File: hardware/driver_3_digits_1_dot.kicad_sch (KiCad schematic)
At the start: 11 parts, among them U4 HV5622PG

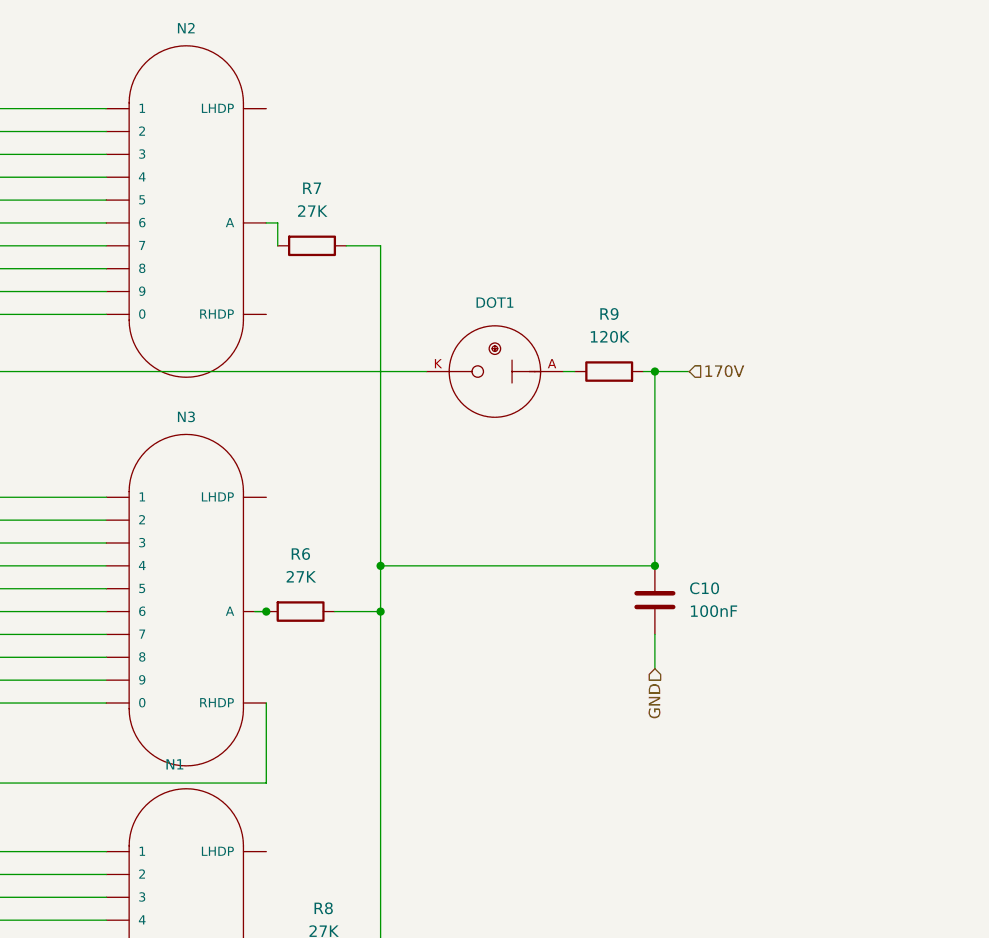
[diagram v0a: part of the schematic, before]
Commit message: Add HT psu.
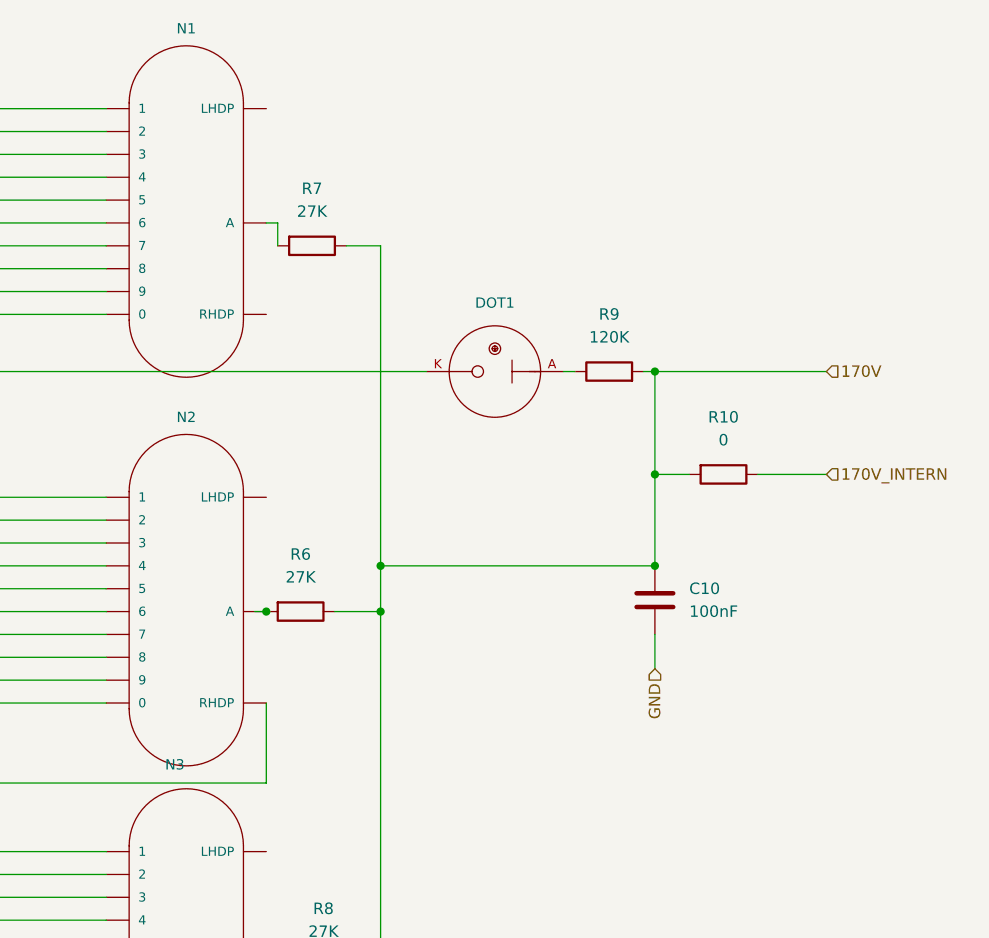
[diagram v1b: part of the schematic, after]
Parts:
- added R10: 0, Resistor_SMD:R_1206_3216Metric, symbol Device:R
- renumbered N2 to N1, N3 to N2, N1 to N3
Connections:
- net 170V: now also R10.2
- new net 170V_INTERN: R10.1
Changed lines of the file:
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@@
+	)
+	(junction
+		(at 182.88 72.39)
+		(diameter 0)
+		(color 0 0 0 0)
+	)
+	(junction
+		(at 152.4 82.55)
+		(diameter 0)
+		(color 0 0 0 0)
 	)
 	(junction
@@
 	)
 	(junction
-		(at 152.4 82.55)
-		(diameter 0)
-		(color 0 0 0 0)
-	)
-	(junction
 		(at 152.4 87.63)
 		(diameter 0)
@@
 	(wire
 		(pts
-			(xy 182.88 60.96) (xy 186.69 60.96)
-		)
-		(stroke
-			(width 0)
-			(type default)
-		)
-	)
-	(wire
-		(pts
 			(xy 148.59 46.99) (xy 152.4 46.99)
 		)
@@
 	(wire
 		(pts
-			(xy 182.88 60.96) (xy 182.88 82.55)
-		)
-		(stroke
-			(width 0)
-			(type default)
-		)
-	)
-	(wire
-		(pts
 			(xy 87.63 85.09) (xy 121.92 85.09)
 		)
@@
 	(wire
 		(pts
+			(xy 182.88 60.96) (xy 182.88 72.39)
+		)
+		(stroke
+			(width 0)
+			(type default)
+		)
+	)
+	(wire
+		(pts
 			(xy 80.01 161.29) (xy 76.2 161.29)
 		)
@@
 	(wire
 		(pts
+			(xy 186.69 72.39) (xy 182.88 72.39)
+		)
+		(stroke
+			(width 0)
+			(type default)
+		)
+	)
+	(wire
+		(pts
 			(xy 87.63 121.92) (xy 121.92 121.92)
 		)
@@
 	(wire
 		(pts
+			(xy 182.88 60.96) (xy 201.93 60.96)
+		)
+		(stroke
+			(width 0)
+			(type default)
+		)
+	)
+	(wire
+		(pts
 			(xy 88.9 49.53) (xy 121.92 49.53)
 		)
@@
 	(wire
 		(pts
+			(xy 194.31 72.39) (xy 201.93 72.39)
+		)
+		(stroke
+			(width 0)
+			(type default)
+		)
+	)
+	(wire
+		(pts
 			(xy 76.2 152.4) (xy 76.2 158.75)
 		)
@@
 		(pts
 			(xy 87.63 106.68) (xy 139.7 106.68)
+		)
+		(stroke
+			(width 0)
+			(type default)
+		)
+	)
+	(wire
+		(pts
+			(xy 182.88 72.39) (xy 182.88 82.55)
 		)
 		(stroke
@@
 		)
 	)
+	(hierarchical_label "170V_INTERN"
+		(shape input)
+		(at 201.93 72.39 0)
+		(effects
+			(font
+				(size 1.27 1.27)
+			)
+			(justify left)
+		)
+	)
 	(hierarchical_label "SPI_SDO"
 		(shape input)
@@
 	(hierarchical_label "170V"
 		(shape input)
-		(at 186.69 60.96 0)
+		(at 201.93 60.96 0)
 		(effects
 			(font
@@
 	)
 	(symbol
+		(lib_id "Device:R")
+		(at 190.5 72.39 270)
+		(unit 1)
+		(exclude_from_sim no)
+		(in_bom yes)
+		(on_board yes)
+		(dnp no)
+		(fields_autoplaced yes)
+		(property "Reference" "R10"
+			(at 190.5 66.04 90)
+			(effects
+				(font
+					(size 1.27 1.27)
+				)
+			)
+		)
+		(property "Value" "0"
+			(at 190.5 68.58 90)
+			(effects
+				(font
+					(size 1.27 1.27)
+				)
+			)
+		)
+		(property "Footprint" "Resistor_SMD:R_1206_3216Metric"
+			(at 190.5 70.612 90)
+			(effects
+				(font
+					(size 1.27 1.27)
+				)
+				(hide yes)
+			)
+		)
+		(property "Datasheet" "~"
+			(at 190.5 72.39 0)
+			(effects
+				(font
+					(size 1.27 1.27)
+				)
+				(hide yes)
+			)
+		)
+		(property "Description" "Resistor"
+			(at 190.5 72.39 0)
+			(effects
+				(font
+					(size 1.27 1.27)
+				)
+				(hide yes)
+			)
+		)
+		(pin "1"
+		)
+		(pin "2"
+		)
+		(instances
+			(project "nixie_clock"
+				(path "/90430e5f-7049-4de8-b92d-f897c4a89819/4b7e288e-9913-4bd2-a435-f0a0986d442d"
+					(reference "R10")
+					(unit 1)
+				)
+			)
+		)
+	)
+	(symbol
 		(lib_id "nixies-us:IN-14")
 		(at 129.54 41.91 0)
@@
 		(on_board yes)
 		(dnp no)
-		(property "Reference" "N2"
+		(property "Reference" "N1"
 			(at 130.81 22.86 0)
 			(effects
@@
 			(project "qw"
 				(path "/90430e5f-7049-4de8-b92d-f897c4a89819/4b7e288e-9913-4bd2-a435-f0a0986d442d"
-					(reference "N2")
+					(reference "N1")
 					(unit 1)
 				)
@@
 		(on_board yes)
 		(dnp no)
-		(property "Reference" "N3"
+		(property "Reference" "N2"
 			(at 130.81 66.04 0)
 			(effects
@@
 			(project "qw"
 				(path "/90430e5f-7049-4de8-b92d-f897c4a89819/4b7e288e-9913-4bd2-a435-f0a0986d442d"
-					(reference "N3")
+					(reference "N2")
 					(unit 1)
 				)
@@
 		(on_board yes)
 		(dnp no)
-		(property "Reference" "N1"
+		(property "Reference" "N3"
 			(at 129.54 104.648 0)
 			(effects
@@
 			(project "qw"
 				(path "/90430e5f-7049-4de8-b92d-f897c4a89819/4b7e288e-9913-4bd2-a435-f0a0986d442d"
-					(reference "N1")
+					(reference "N3")
 					(unit 1)
 				)

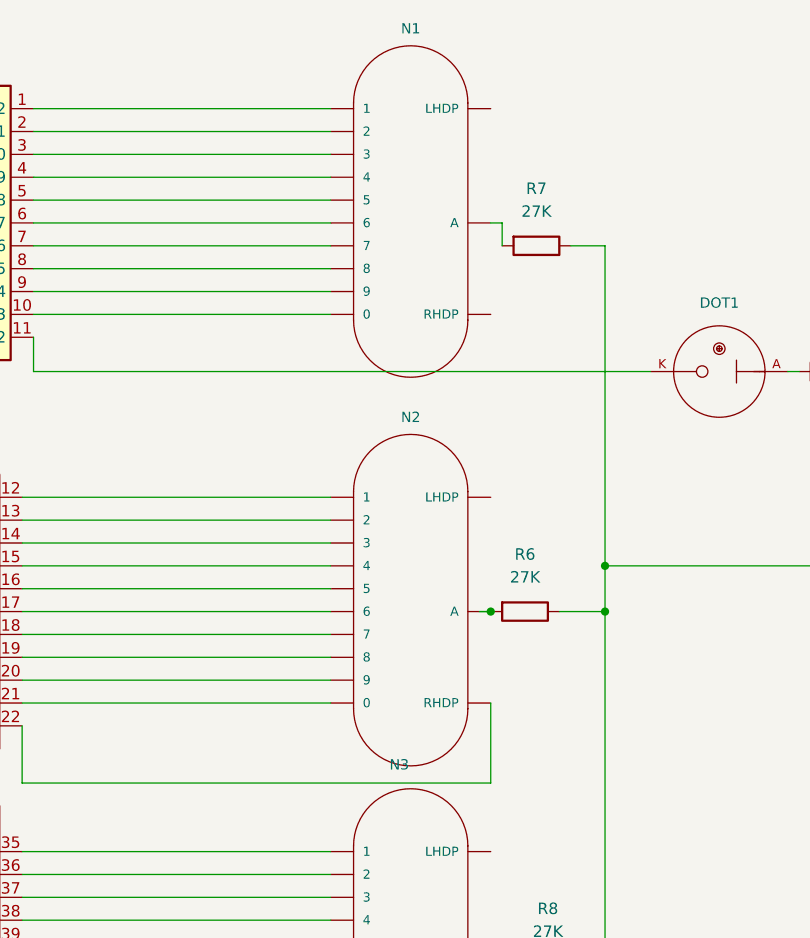
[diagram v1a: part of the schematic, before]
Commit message: Rename nixie's names to have the right order.
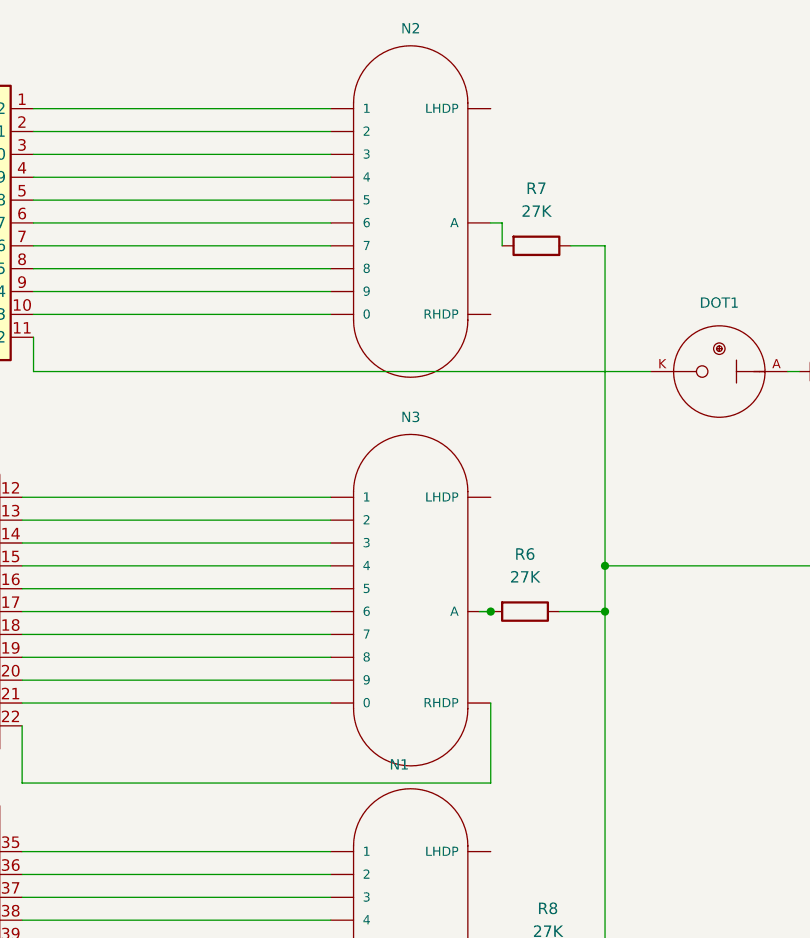
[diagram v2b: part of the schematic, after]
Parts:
- renumbered N3 to N1, N1 to N2, N2 to N3
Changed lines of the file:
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@@
 		(on_board yes)
 		(dnp no)
-		(property "Reference" "N1"
+		(property "Reference" "N2"
 			(at 130.81 22.86 0)
 			(effects
@@
 			(project "qw"
 				(path "/90430e5f-7049-4de8-b92d-f897c4a89819/4b7e288e-9913-4bd2-a435-f0a0986d442d"
-					(reference "N1")
+					(reference "N2")
 					(unit 1)
 				)
@@
 		(on_board yes)
 		(dnp no)
-		(property "Reference" "N2"
+		(property "Reference" "N3"
 			(at 130.81 66.04 0)
 			(effects
@@
 			(project "qw"
 				(path "/90430e5f-7049-4de8-b92d-f897c4a89819/4b7e288e-9913-4bd2-a435-f0a0986d442d"
-					(reference "N2")
+					(reference "N3")
 					(unit 1)
 				)
@@
 		(on_board yes)
 		(dnp no)
-		(property "Reference" "N3"
+		(property "Reference" "N1"
 			(at 129.54 104.648 0)
 			(effects
@@
 			(project "qw"
 				(path "/90430e5f-7049-4de8-b92d-f897c4a89819/4b7e288e-9913-4bd2-a435-f0a0986d442d"
-					(reference "N3")
-					(unit 1)
-				)
+					(reference "N1")
+					(unit 1)
+				)

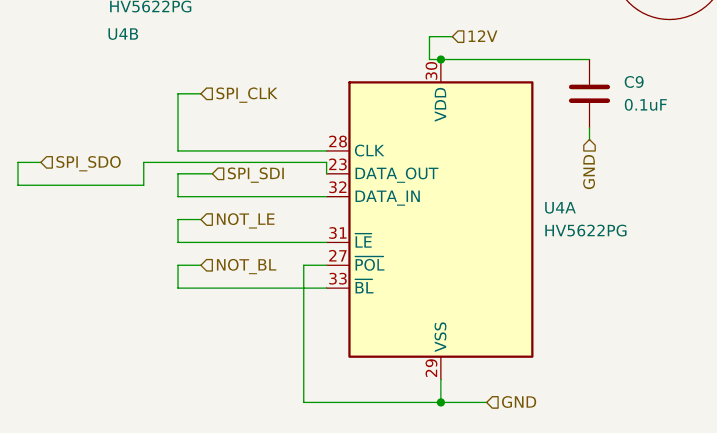
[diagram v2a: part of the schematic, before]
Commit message: Remove POLarity setup, needs 12V to be not reversed.
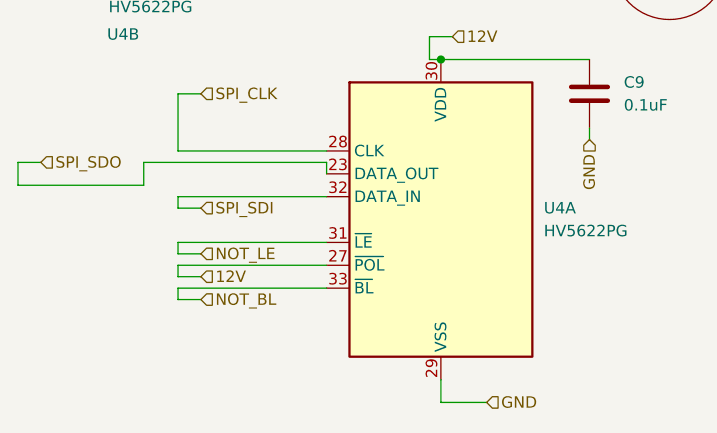
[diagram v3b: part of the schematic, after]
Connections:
- net 12V: now also U4.27 (~{POL})
- net GND: no longer U4.27 (~{POL})
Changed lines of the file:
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@@
-	)
-	(junction
-		(at 105.41 186.69)
-		(diameter 0)
-		(color 0 0 0 0)
 	)
 	(junction
@@
 	(wire
 		(pts
-			(xy 78.74 171.45) (xy 76.2 171.45)
+			(xy 78.74 175.26) (xy 76.2 175.26)
 		)
 		(stroke
@@
 	(wire
 		(pts
-			(xy 76.2 166.37) (xy 76.2 168.91)
+			(xy 76.2 170.18) (xy 76.2 168.91)
 		)
 		(stroke
@@
 	(wire
 		(pts
-			(xy 80.01 161.29) (xy 76.2 161.29)
+			(xy 78.74 165.1) (xy 76.2 165.1)
 		)
 		(stroke
@@
 	(wire
 		(pts
-			(xy 90.17 171.45) (xy 92.71 171.45)
+			(xy 92.71 171.45) (xy 76.2 171.45)
 		)
 		(stroke
@@
 	(wire
 		(pts
+			(xy 76.2 172.72) (xy 76.2 171.45)
+		)
+		(stroke
+			(width 0)
+			(type default)
+		)
+	)
+	(wire
+		(pts
 			(xy 87.63 80.01) (xy 121.92 80.01)
 		)
@@
 	(wire
 		(pts
-			(xy 90.17 186.69) (xy 105.41 186.69)
-		)
-		(stroke
-			(width 0)
-			(type default)
-		)
-	)
-	(wire
-		(pts
 			(xy 88.9 60.96) (xy 88.9 57.15)
 		)
@@
 	(wire
 		(pts
-			(xy 76.2 161.29) (xy 76.2 163.83)
+			(xy 76.2 165.1) (xy 76.2 163.83)
 		)
 		(stroke
@@
 	(wire
 		(pts
-			(xy 90.17 171.45) (xy 90.17 186.69)
-		)
-		(stroke
-			(width 0)
-			(type default)
-		)
-	)
-	(wire
-		(pts
 			(xy 87.63 97.79) (xy 121.92 97.79)
 		)
@@
 	(wire
 		(pts
+			(xy 76.2 172.72) (xy 78.74 172.72)
+		)
+		(stroke
+			(width 0)
+			(type default)
+		)
+	)
+	(wire
+		(pts
 			(xy 182.88 72.39) (xy 182.88 82.55)
 		)
@@
 	(wire
 		(pts
-			(xy 76.2 171.45) (xy 76.2 173.99)
+			(xy 76.2 175.26) (xy 76.2 173.99)
 		)
 		(stroke
@@
 	(wire
 		(pts
-			(xy 78.74 166.37) (xy 76.2 166.37)
+			(xy 76.2 170.18) (xy 78.74 170.18)
 		)
 		(stroke
@@
 	(hierarchical_label "SPI_SDI"
 		(shape input)
-		(at 80.01 161.29 0)
+		(at 78.74 165.1 0)
 		(effects
 			(font
@@
 	(hierarchical_label "NOT_LE"
 		(shape input)
-		(at 78.74 166.37 0)
+		(at 78.74 170.18 0)
 		(effects
 			(font
@@
 	(hierarchical_label "NOT_BL"
 		(shape input)
-		(at 78.74 171.45 0)
+		(at 78.74 175.26 0)
 		(effects
 			(font
@@
 		)
 	)
+	(hierarchical_label "12V"
+		(shape input)
+		(at 78.74 172.72 0)
+		(effects
+			(font
+				(size 1.27 1.27)
+			)
+			(justify left)
+		)
+	)

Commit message: C15, C13, C9  changed to 805 form factor. Removed tracks under capacitors.
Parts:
- C9: footprint Capacitor_SMD:C_1206_3216Metric -> Resistor_SMD:R_0805_2012Metric
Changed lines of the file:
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@@
 			)
 		)
-		(property "Footprint" "Capacitor_SMD:C_1206_3216Metric"
+		(property "Footprint" "Resistor_SMD:R_0805_2012Metric"
 			(at 120.9548 148.59 0)
 			(effects
